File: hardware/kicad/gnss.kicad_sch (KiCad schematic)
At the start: 7 parts, among them U10 L86-M33

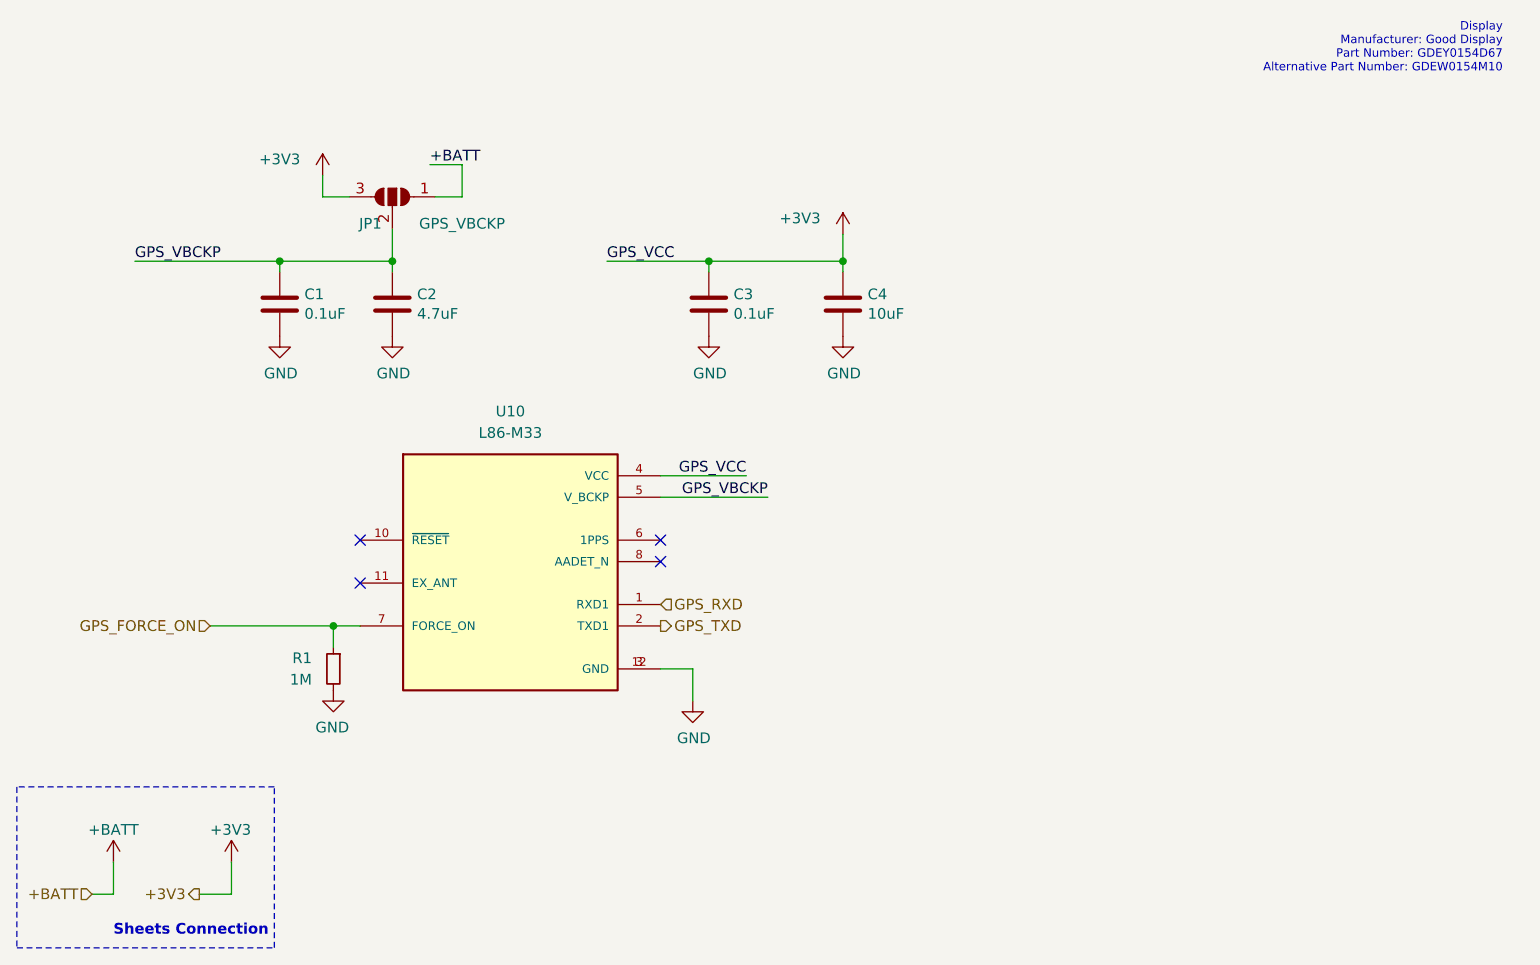
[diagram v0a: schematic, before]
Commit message: update schematics with gnss
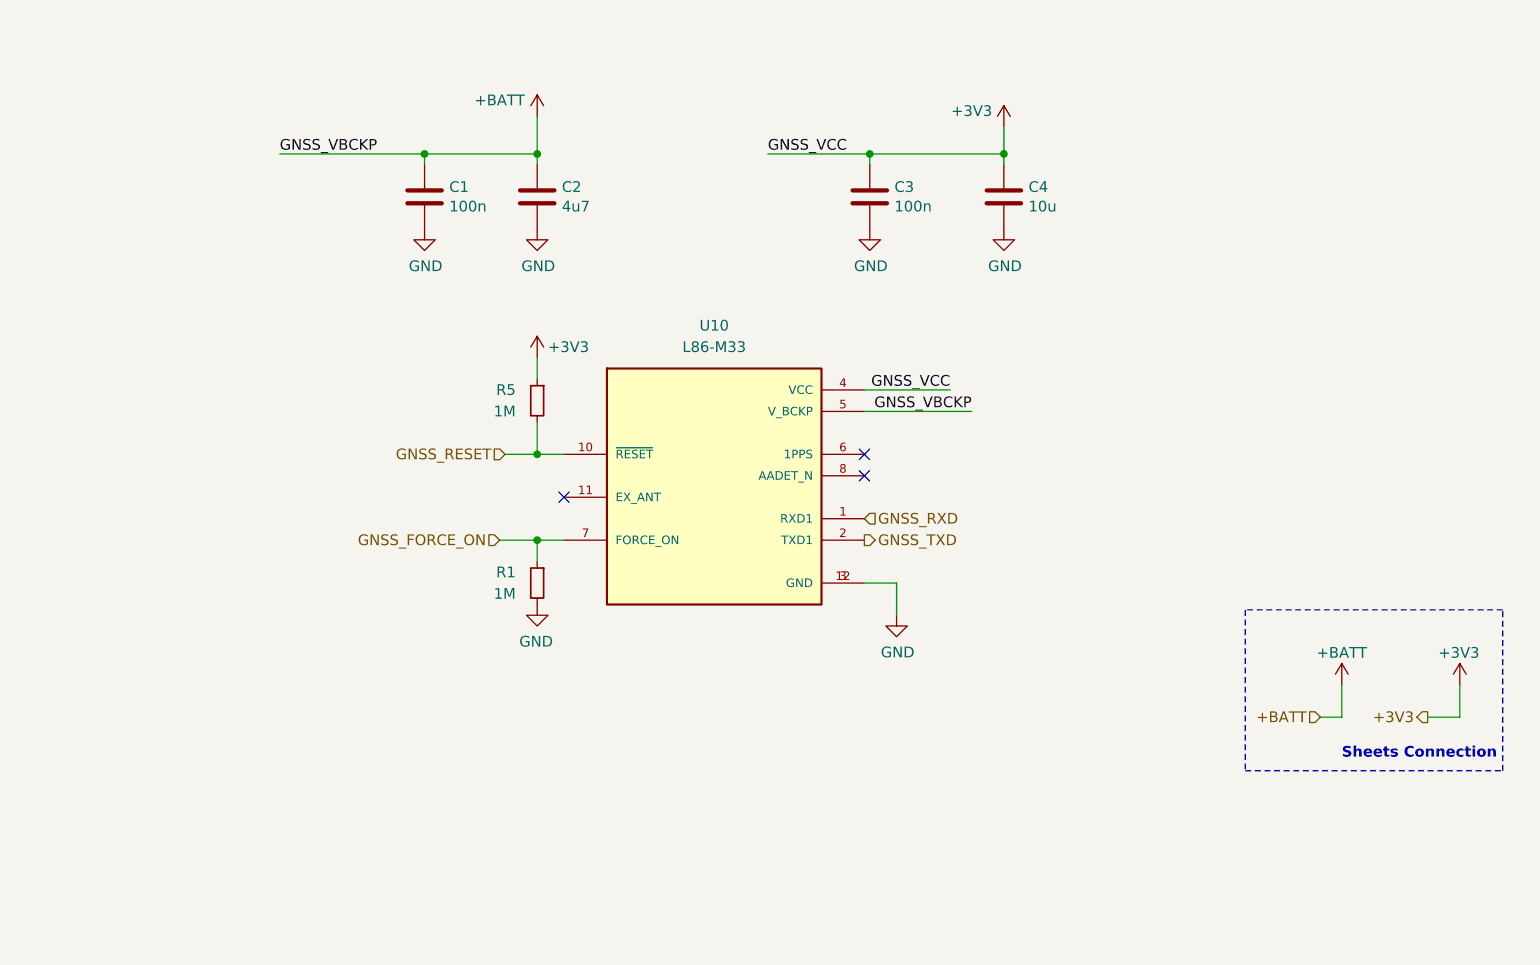
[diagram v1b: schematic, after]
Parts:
- removed JP1: GPS_VBCKP, Jumper:SolderJumper-3_P1.3mm_Open_RoundedPad1.0x1.5mm_NumberLabels, symbol Jumper:SolderJumper_3_Open
- added R5: 1M, Resistor_SMD:R_0603_1608Metric, symbol Device:R_Small
- C1, C3: value 0.1uF -> 100n
- C2: value 4.7uF -> 4u7
- C4: value 10uF -> 10u
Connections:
- net GPS_VBCKP is gone; now on net +BATT: C1.1, C2.1, U10.5 (V_BCKP)
- net +3V3: now also R5.1
- net GNSS_RESET: now reaches U10.10 (~{RESET})
- net GNSS_RESET: now also R5.2
- net GPS_FORCE_ON renamed GNSS_FORCE_ON
- net GPS_RXD renamed GNSS_RXD
- net GPS_TXD renamed GNSS_TXD
- no-connect marks 4 -> 3
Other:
- note removed: "Display Manufacturer: Good Display Part Number: GDEY0154D67 Alternative Part Number: GDEW0154M10"
- moved on the sheet: C1, C2, C3, C4, R1, U10

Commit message: update pcb
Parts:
- removed R5: 1M, Resistor_SMD:R_0603_1608Metric, symbol Device:R_Small
- R1: footprint Resistor_SMD:R_0603_1608Metric -> Resistor_SMD:R_0402_1005Metric
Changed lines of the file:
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@@
-		(color 0 0 0 0)
-	)
-	(junction
-		(at 81.915 64.77)
-		(diameter 0)
 		(color 0 0 0 0)
 	)
@@
 	(wire
 		(pts
-			(xy 81.915 64.77) (xy 85.09 64.77)
-		)
-		(stroke
-			(width 0)
-			(type default)
-		)
-	)
-	(wire
-		(pts
 			(xy 51.435 29.21) (xy 68.58 29.21)
 		)
@@
 	(wire
 		(pts
-			(xy 81.915 53.34) (xy 81.915 55.88)
-		)
-		(stroke
-			(width 0)
-			(type default)
-		)
-	)
-	(wire
-		(pts
 			(xy 137.16 29.21) (xy 137.16 30.48)
 		)
@@
 	(wire
 		(pts
-			(xy 81.915 60.96) (xy 81.915 64.77)
-		)
-		(stroke
-			(width 0)
-			(type default)
-		)
-	)
-	(wire
-		(pts
 			(xy 81.915 74.93) (xy 81.915 77.47)
 		)
@@
 	(wire
 		(pts
-			(xy 78.105 64.77) (xy 81.915 64.77)
+			(xy 78.105 64.77) (xy 85.09 64.77)
 		)
 		(stroke
@@
 			)
 		)
-		(property "Footprint" "Resistor_SMD:R_0603_1608Metric"
+		(property "Footprint" "Resistor_SMD:R_0402_1005Metric"
 			(at 81.915 80.01 0)
 			(effects
@@
 		)
 		(property "Description" ""
+			(at 81.915 80.01 0)
+			(effects
+				(font
+					(size 1.27 1.27)
+				)
+				(hide yes)
+			)
+		)
+		(property "Manufacturer" ""
+			(at 81.915 80.01 0)
+			(effects
+				(font
+					(size 1.27 1.27)
+				)
+				(hide yes)
+			)
+		)
+		(property "Manufacturer Part Number" ""
+			(at 81.915 80.01 0)
+			(effects
+				(font
+					(size 1.27 1.27)
+				)
+				(hide yes)
+			)
+		)
+		(property "Distributor" ""
+			(at 81.915 80.01 0)
+			(effects
+				(font
+					(size 1.27 1.27)
+				)
+				(hide yes)
+			)
+		)
+		(property "Distributor Part Number" ""
+			(at 81.915 80.01 0)
+			(effects
+				(font
+					(size 1.27 1.27)
+				)
+				(hide yes)
+			)
+		)
+		(property "Distributor Link" ""
 			(at 81.915 80.01 0)
 			(effects
@@
 			)
 		)
+		(property "Manufacturer" ""
+			(at 121.285 34.29 0)
+			(effects
+				(font
+					(size 1.27 1.27)
+				)
+				(hide yes)
+			)
+		)
+		(property "Manufacturer Part Number" ""
+			(at 121.285 34.29 0)
+			(effects
+				(font
+					(size 1.27 1.27)
+				)
+				(hide yes)
+			)
+		)
+		(property "Distributor" ""
+			(at 121.285 34.29 0)
+			(effects
+				(font
+					(size 1.27 1.27)
+				)
+				(hide yes)
+			)
+		)
+		(property "Distributor Part Number" ""
+			(at 121.285 34.29 0)
+			(effects
+				(font
+					(size 1.27 1.27)
+				)
+				(hide yes)
+			)
+		)
+		(property "Distributor Link" ""
+			(at 121.285 34.29 0)
+			(effects
+				(font
+					(size 1.27 1.27)
+				)
+				(hide yes)
+			)
+		)
 		(pin "1"
 		)
@@
 				(path "/59b4123e-c7be-466b-a5db-658b8f0c1171/f9cd082b-cac9-43d6-8c9f-f1ebaeb9f81d"
 					(reference "C44")
-					(unit 1)
-				)
-			)
-		)
-	)
-	(symbol
-		(lib_id "Device:R_Small")
-		(at 81.915 58.42 0)
-		(mirror y)
-		(unit 1)
-		(exclude_from_sim no)
-		(in_bom yes)
-		(on_board yes)
-		(dnp no)
-		(property "Reference" "R5"
-			(at 79.375 57.1499 0)
-			(effects
-				(font
-					(size 1.27 1.27)
-				)
-				(justify left)
-			)
-		)
-		(property "Value" "1M"
-			(at 79.375 59.6899 0)
-			(effects
-				(font
-					(size 1.27 1.27)
-				)
-				(justify left)
-			)
-		)
-		(property "Footprint" "Resistor_SMD:R_0603_1608Metric"
-			(at 81.915 58.42 0)
-			(effects
-				(font
-					(size 1.27 1.27)
-				)
-				(hide yes)
-			)
-		)
-		(property "Datasheet" "~"
-			(at 81.915 58.42 0)
-			(effects
-				(font
-					(size 1.27 1.27)
-				)
-				(hide yes)
-			)
-		)
-		(property "Description" ""
-			(at 81.915 58.42 0)
-			(effects
-				(font
-					(size 1.27 1.27)
-				)
-				(hide yes)
-			)
-		)
-		(pin "1"
-		)
-		(pin "2"
-		)
-		(instances
-			(project "atlas"
-				(path "/59b4123e-c7be-466b-a5db-658b8f0c1171/f9cd082b-cac9-43d6-8c9f-f1ebaeb9f81d"
-					(reference "R5")
 					(unit 1)
 				)
@@
 			)
 		)
+		(property "Manufacturer" ""
+			(at 81.915 34.29 0)
+			(effects
+				(font
+					(size 1.27 1.27)
+				)
+				(hide yes)
+			)
+		)
+		(property "Manufacturer Part Number" ""
+			(at 81.915 34.29 0)
+			(effects
+				(font
+					(size 1.27 1.27)
+				)
+				(hide yes)
+			)
+		)
+		(property "Distributor" ""
+			(at 81.915 34.29 0)
+			(effects
+				(font
+					(size 1.27 1.27)
+				)
+				(hide yes)
+			)
+		)
+		(property "Distributor Part Number" ""
+			(at 81.915 34.29 0)
+			(effects
+				(font
+					(size 1.27 1.27)
+				)
+				(hide yes)
+			)
+		)
+		(property "Distributor Link" ""
+			(at 81.915 34.29 0)
+			(effects
+				(font
+					(size 1.27 1.27)
+				)
+				(hide yes)
+			)
+		)
 		(pin "1"
 		)
@@
 			)
 		)
+		(property "Manufacturer" ""
+			(at 137.16 34.29 0)
+			(effects
+				(font
+					(size 1.27 1.27)
+				)
+				(hide yes)
+			)
+		)
+		(property "Manufacturer Part Number" ""
+			(at 137.16 34.29 0)
+			(effects
+				(font
+					(size 1.27 1.27)
+				)
+				(hide yes)
+			)
+		)
+		(property "Distributor" ""
+			(at 137.16 34.29 0)
+			(effects
+				(font
+					(size 1.27 1.27)
+				)
+				(hide yes)
+			)
+		)
+		(property "Distributor Part Number" ""
+			(at 137.16 34.29 0)
+			(effects
+				(font
+					(size 1.27 1.27)
+				)
+				(hide yes)
+			)
+		)
+		(property "Distributor Link" ""
+			(at 137.16 34.29 0)
+			(effects
+				(font
+					(size 1.27 1.27)
+				)
+				(hide yes)
+			)
+		)
 		(pin "1"
 		)
@@
 		)
 		(property "Description" ""
+			(at 68.58 34.29 0)
+			(effects
+				(font
+					(size 1.27 1.27)
+				)
+				(hide yes)
+			)
+		)
+		(property "Manufacturer" ""
+			(at 68.58 34.29 0)
+			(effects
+				(font
+					(size 1.27 1.27)
+				)
+				(hide yes)
+			)
+		)
+		(property "Manufacturer Part Number" ""
+			(at 68.58 34.29 0)
+			(effects
+				(font
+					(size 1.27 1.27)
+				)
+				(hide yes)
+			)
+		)
+		(property "Distributor" ""
+			(at 68.58 34.29 0)
+			(effects
+				(font
+					(size 1.27 1.27)
+				)
+				(hide yes)
+			)
+		)
+		(property "Distributor Part Number" ""
+			(at 68.58 34.29 0)
+			(effects
+				(font
+					(size 1.27 1.27)
+				)
+				(hide yes)
+			)
+		)
+		(property "Distributor Link" ""
 			(at 68.58 34.29 0)
 			(effects
@@
 					(unit 1)
 				)
-			)
-		)
-	)
-	(symbol
-		(lib_id "power:+3V3")
-		(at 81.915 53.34 0)
-		(mirror y)
-		(unit 1)
-		(exclude_from_sim no)
-		(in_bom yes)
-		(on_board yes)
-		(dnp no)
-		(property "Reference" "#PWR01"
-			(at 81.915 57.15 0)
-			(effects
-				(font
-					(size 1.27 1.27)
-				)
-				(hide yes)
-			)
-		)
-		(property "Value" "+3V3"
-			(at 83.185 52.07 0)
-			(effects
-				(font
-					(size 1.27 1.27)
-				)
-				(justify right)
-			)
-		)
-		(property "Footprint" ""
-			(at 81.915 53.34 0)
-			(effects
-				(font
-					(size 1.27 1.27)
-				)
-				(hide yes)
-			)
-		)
-		(property "Datasheet" ""
-			(at 81.915 53.34 0)
-			(effects
-				(font
-					(size 1.27 1.27)
-				)
-				(hide yes)
-			)
-		)
-		(property "Description" ""
-			(at 81.915 53.34 0)
-			(effects
-				(font
-					(size 1.27 1.27)
-				)
-				(hide yes)
-			)
-		)
-		(pin "1"
-		)
-		(instances
-			(project "atlas"
-				(path "/59b4123e-c7be-466b-a5db-658b8f0c1171/f9cd082b-cac9-43d6-8c9f-f1ebaeb9f81d"
-					(reference "#PWR01")
-					(unit 1)
-				)

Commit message: clean-up
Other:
- title: GPS -> GNSS
- moved on the sheet: C1, C2, C3, C4

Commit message: update schematics info
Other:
- title: GNSS -> Teapotlabs Atlas
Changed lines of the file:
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@@
 	(paper "A5")
 	(title_block
-		(title "GNSS")
-		(date "2024-04-06")
-		(rev "5")
+		(title "Teapotlabs Atlas")
+		(date "2024-10-25")
+		(rev "1")
 		(company "Teapot Laboratories")
 	)
